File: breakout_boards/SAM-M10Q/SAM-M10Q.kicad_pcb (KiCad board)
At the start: 2 copper layers, 34.5 x 31.2 mm, 10 parts, among them J1 Conn_01x06_Pin, U1 SAM-M10Q

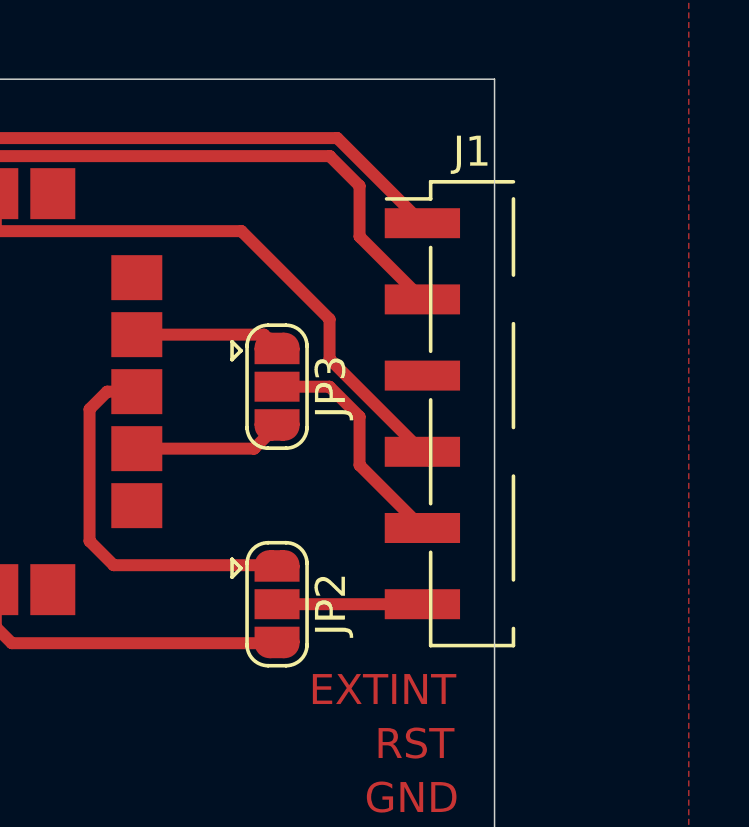
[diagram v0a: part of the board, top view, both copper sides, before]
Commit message: made new M10Q footprint and added a diode
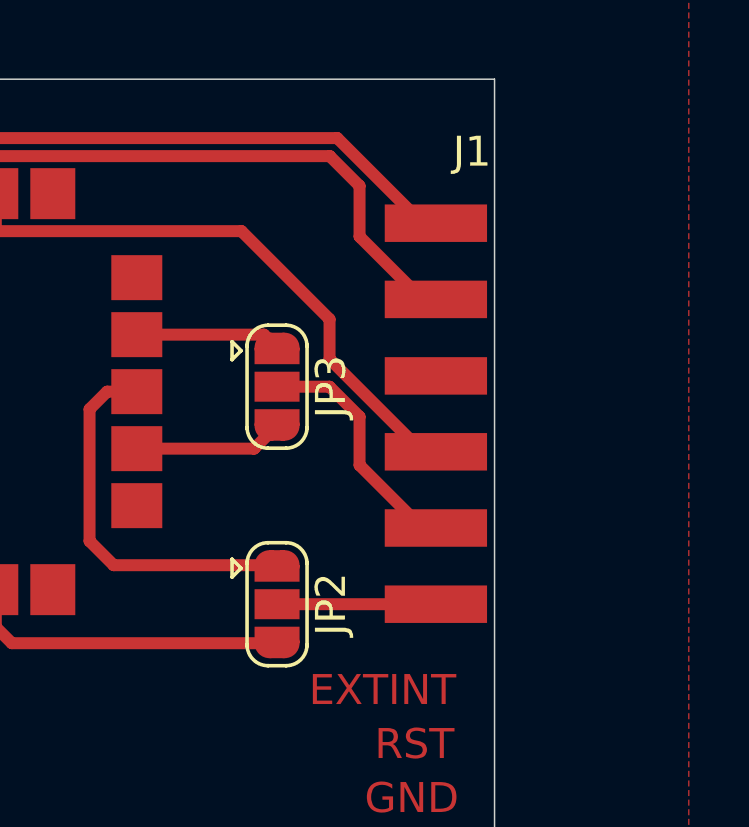
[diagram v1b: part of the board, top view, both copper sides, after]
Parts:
- J1: footprint _footprints:PinHeader_1x06_P2.54mm_Vertical_SMD_Pin1Left -> _footprints:JST_XH_1x06_P2.54mm_Horizontal
